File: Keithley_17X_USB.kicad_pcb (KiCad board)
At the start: 2 copper layers, 70.5 x 44 mm, 42 parts, among them J1 USB_B, J2 SIGNAL INPUT, J3 PROG, U1 TLP281-4, U2 TLP281-4, U3 MIC5504-3.3YM5, U4 MSP430FR2110, U5 FT230XS

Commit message: update silkscreen
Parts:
- added G***: LOGO, PL_logo:logo_height_10mm, F.Cu at (98.5, 82.0)
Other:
- board text added: "*"
- board text added: "5V"
- board text added: "Keithley 17X USB Adapter"
- board text added: "Keithley J1008 Connection"
- board text added: "March 2019"
- board text added: "RX"
- board text added: "TX"
- board text added: "github.com/sdp8483/Keithley_17X_USB"
- board text removed: "To Keithley J1008"

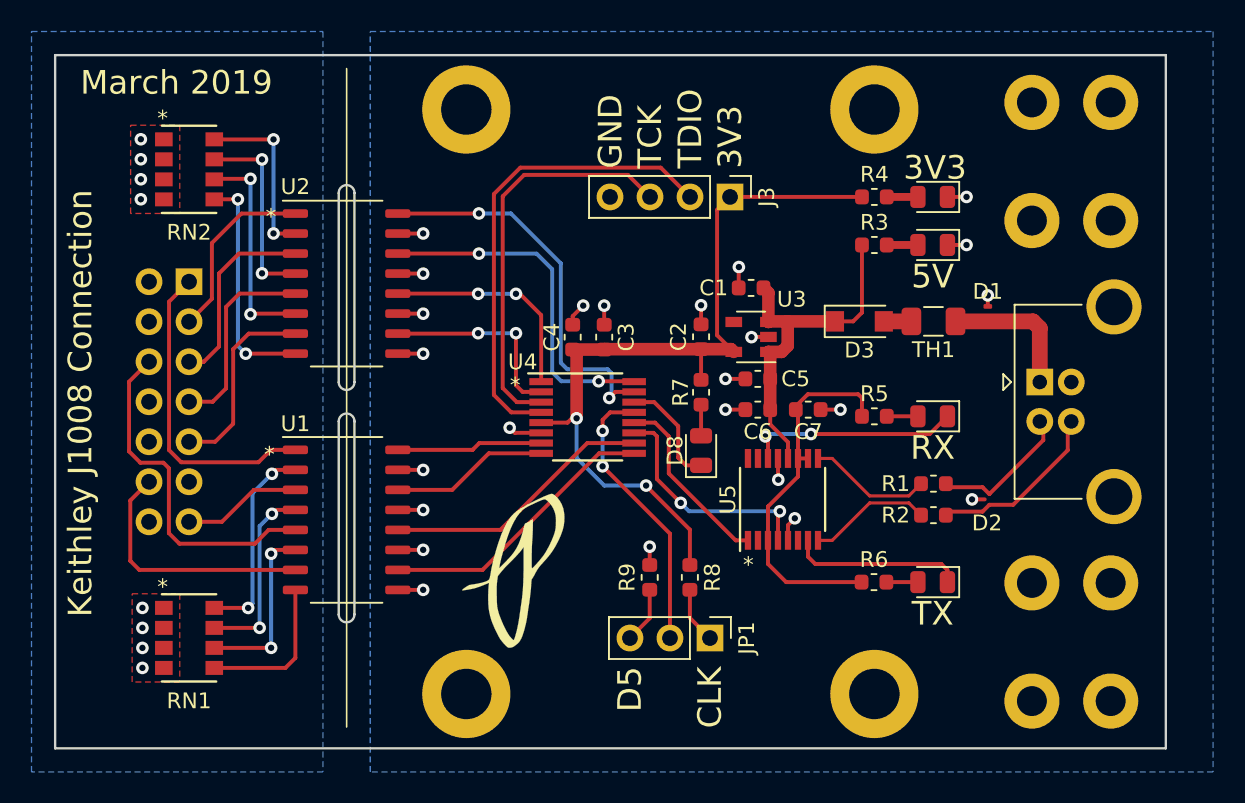
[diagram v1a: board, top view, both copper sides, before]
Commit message: minor silkscreen cleanup
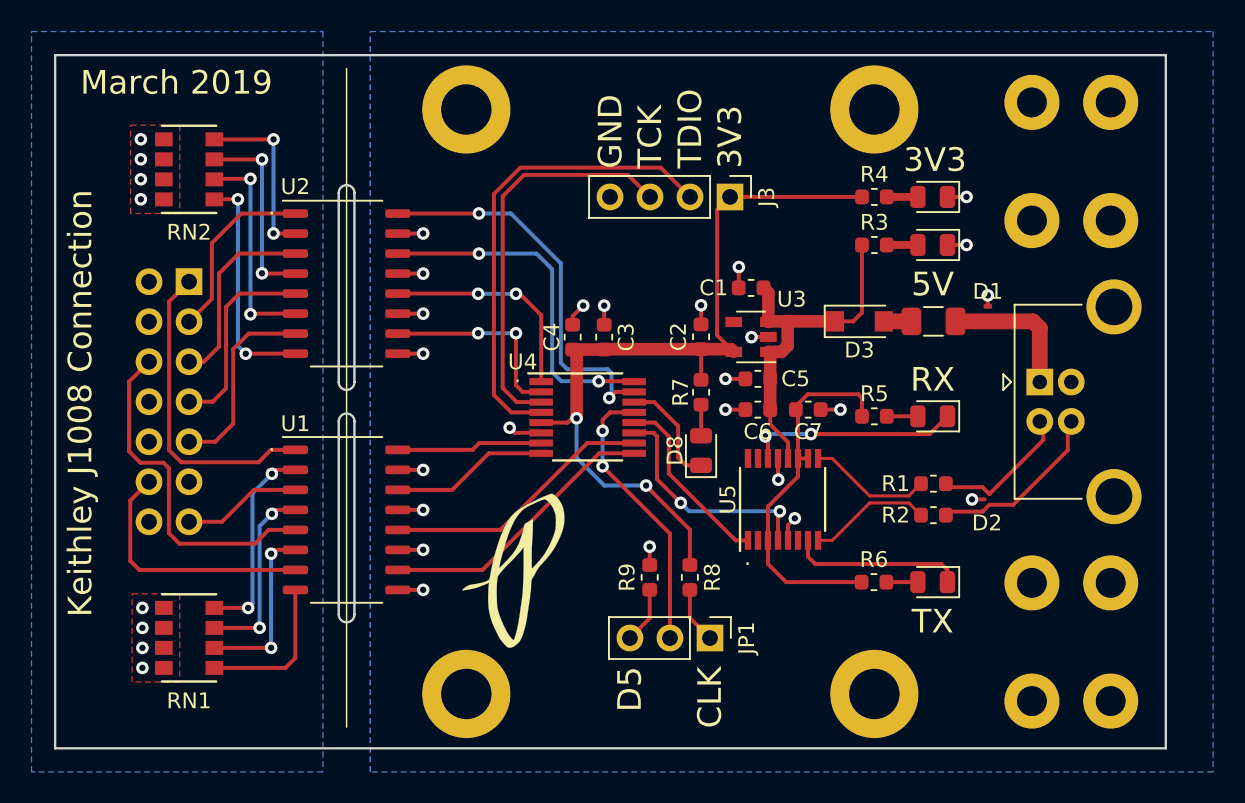
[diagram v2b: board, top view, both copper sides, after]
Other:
- board text added: "."
- board text added: "Sam Perry"
- board text removed: "*"
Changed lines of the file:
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@@
   (general
     (thickness 1.6)
-    (drawings 140)
+    (drawings 141)
     (tracks 375)
     (zones 0)
@@
   )
   (setup
-    (last_trace_width 0.5)
+    (last_trace_width 0.25)
     (user_trace_width 0.5)
     (user_trace_width 0.8)
@@
       (effects (font (size 0.127 0.127) (thickness 0.002)))
     )
-    (fp_text user * (at -1.6764 -3.2385) (layer F.SilkS)
+    (fp_text user * (at -1.6764 -3.2385) (layer F.SilkS) hide
       (effects (font (size 1 1) (thickness 0.15)))
     )
@@
       (effects (font (size 1 1) (thickness 0.15)))
     )
-    (fp_text user * (at -1.6764 -3.2385) (layer F.SilkS)
+    (fp_text user * (at -1.6764 -3.2385) (layer F.SilkS) hide
       (effects (font (size 1 1) (thickness 0.15)))
     )
@@
     (tags resistor)
     (attr smd)
-    (fp_text reference TH1 (at 0 1.8) (layer F.SilkS)
+    (fp_text reference TH1 (at 0 0) (layer F.SilkS) hide
       (effects (font (size 1 1) (thickness 0.15)))
     )
@@
       (xy 2.424964 -4.901719) (xy 2.473487 -4.908822) (xy 2.555224 -4.885326)) (layer F.SilkS) (width 0.01))
   )
-  (gr_text * (at 83.1 74.6) (layer F.SilkS)
+  (gr_text "Sam Perry" (at 76.3 91.1) (layer B.SilkS)
+    (effects (font (size 1.5 1.5) (thickness 0.3)) (justify mirror))
+  )
+  (gr_text . (at 83.25 73.9) (layer F.SilkS)
     (effects (font (size 1 1) (thickness 0.25)))
   )
-  (gr_text * (at 83.2 59.5) (layer F.SilkS)
+  (gr_text . (at 83.25 58.9) (layer F.SilkS)
     (effects (font (size 1 1) (thickness 0.25)))
   )
@@
     (effects (font (size 1.2 1.2) (thickness 0.17)) (justify mirror))
   )
-  (gr_text * (at 113.5 81.6) (layer F.SilkS)
+  (gr_text . (at 113.45 81.15) (layer F.SilkS)
     (effects (font (size 1 1) (thickness 0.25)))
   )
-  (gr_text * (at 98.7 70.2) (layer F.SilkS)
+  (gr_text . (at 98.85 69.55) (layer F.SilkS)
     (effects (font (size 1 1) (thickness 0.25)))
   )
@@
     (effects (font (size 1.5 1.5) (thickness 0.3)))
   )
-  (gr_text 3V3 (at 125.35 56.4) (layer F.SilkS)
+  (gr_text 3V3 (at 125.35 55.9) (layer F.SilkS)
     (effects (font (size 1.5 1.5) (thickness 0.3)))
   )
-  (gr_text 5V (at 125.2 63.3) (layer F.SilkS)
+  (gr_text 5V (at 125.2 63.8) (layer F.SilkS)
     (effects (font (size 1.5 1.5) (thickness 0.3)))
   )
-  (gr_text RX (at 125.2 74.175) (layer F.SilkS)
+  (gr_text RX (at 125.2 69.85) (layer F.SilkS)
     (effects (font (size 1.5 1.5) (thickness 0.3)))
   )
-  (gr_text TX (at 125.2 84.7) (layer F.SilkS)
+  (gr_text TX (at 125.2 85.2) (layer F.SilkS)
     (effects (font (size 1.5 1.5) (thickness 0.3)))
   )

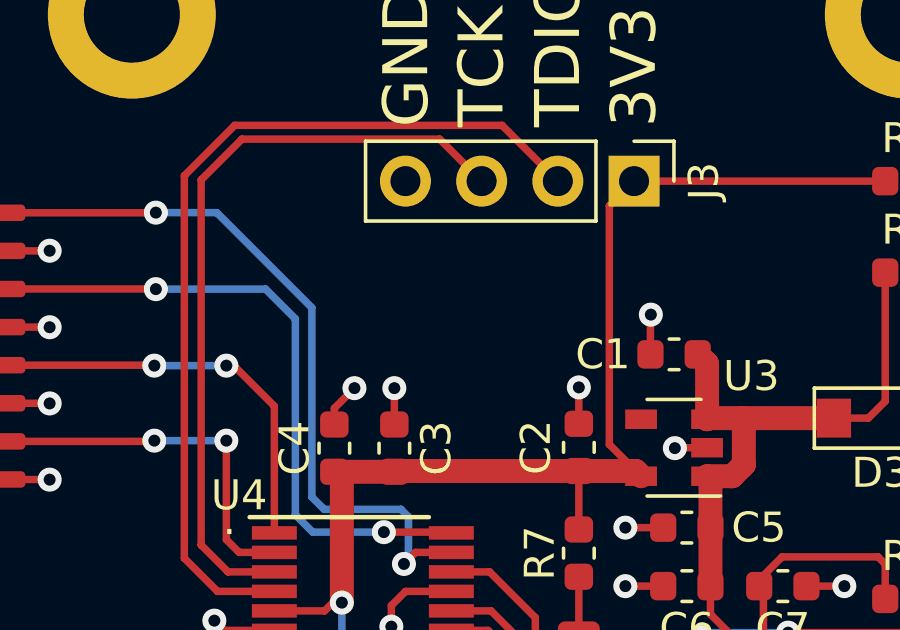
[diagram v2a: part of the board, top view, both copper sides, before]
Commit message: add bluebird logo
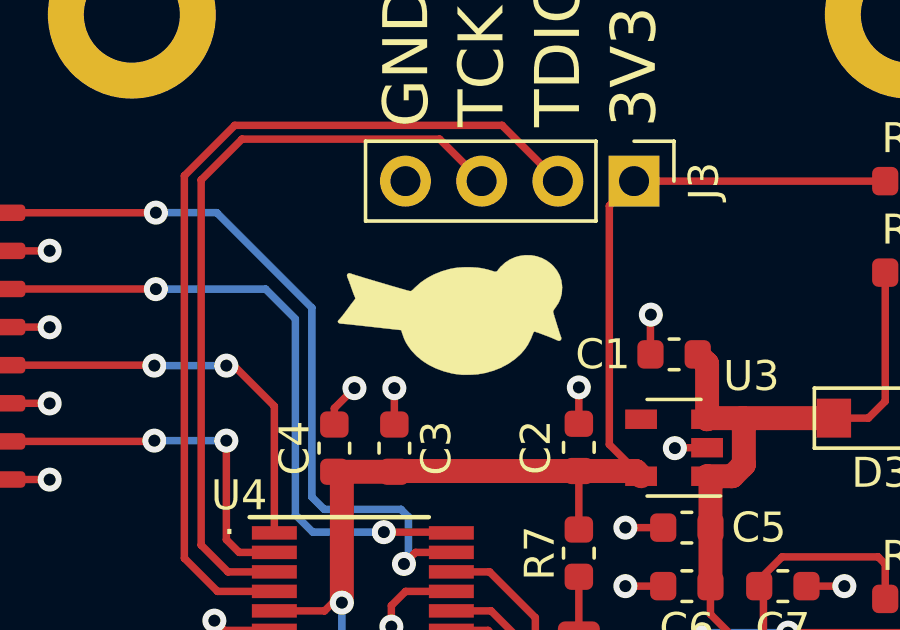
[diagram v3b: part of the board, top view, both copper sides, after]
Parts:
- added G***: LOGO, BB_logo:BB_logo_HxW_4x7.5mm, F.Cu at (106.2, 62.7)
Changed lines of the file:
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@@
     (tracks 375)
     (zones 0)
-    (modules 43)
+    (modules 44)
     (nets 51)
   )
@@
       (xy 2.424964 -4.901719) (xy 2.473487 -4.908822) (xy 2.555224 -4.885326)) (layer F.SilkS) (width 0.01))
   )
+  (module BB_logo:BB_logo_HxW_4x7.5mm (layer F.Cu)
+    (at 106.2 62.7)
+    (fp_text reference G*** (at 0 0) (layer F.SilkS) hide
+      (effects (font (size 1.524 1.524) (thickness 0.3)))
+    )
+    (fp_text value LOGO (at 0.75 0) (layer F.SilkS) hide
+      (effects (font (size 1.524 1.524) (thickness 0.3)))
+    )
+    (fp_poly (pts (xy 2.713927 -1.978373) (xy 2.895506 -1.945528) (xy 3.070555 -1.885268) (xy 3.235321 -1.797572)
+      (xy 3.38605 -1.682422) (xy 3.459178 -1.610019) (xy 3.577218 -1.461306) (xy 3.662911 -1.304796)
+      (xy 3.717434 -1.137514) (xy 3.741962 -0.956484) (xy 3.743678 -0.889961) (xy 3.73089 -0.709742)
+      (xy 3.691076 -0.545202) (xy 3.622063 -0.390068) (xy 3.521675 -0.23807) (xy 3.514363 -0.2286)
+      (xy 3.465913 -0.159606) (xy 3.443954 -0.111185) (xy 3.443268 -0.093134) (xy 3.45579 -0.045345)
+      (xy 3.475787 0.024796) (xy 3.501503 0.111666) (xy 3.531183 0.209644) (xy 3.56307 0.313107)
+      (xy 3.595407 0.416431) (xy 3.626438 0.513995) (xy 3.654407 0.600176) (xy 3.677557 0.669352)
+      (xy 3.694133 0.715899) (xy 3.701189 0.732569) (xy 3.718155 0.788501) (xy 3.704623 0.836223)
+      (xy 3.671061 0.865458) (xy 3.640667 0.874227) (xy 3.603186 0.866306) (xy 3.566375 0.849917)
+      (xy 3.511462 0.824622) (xy 3.437823 0.793194) (xy 3.350839 0.757671) (xy 3.255891 0.720093)
+      (xy 3.158361 0.682501) (xy 3.063629 0.646933) (xy 2.977078 0.615428) (xy 2.904088 0.590028)
+      (xy 2.850041 0.572771) (xy 2.820318 0.565696) (xy 2.816927 0.565872) (xy 2.791362 0.588472)
+      (xy 2.78272 0.604982) (xy 2.699594 0.814185) (xy 2.604955 0.996877) (xy 2.494918 1.159546)
+      (xy 2.365602 1.308678) (xy 2.35488 1.319637) (xy 2.162621 1.49097) (xy 1.946322 1.640562)
+      (xy 1.70905 1.766977) (xy 1.453869 1.86878) (xy 1.183844 1.944537) (xy 0.922867 1.990257)
+      (xy 0.881116 1.993977) (xy 0.818728 1.997654) (xy 0.742836 2.001076) (xy 0.660579 2.004033)
+      (xy 0.579091 2.006315) (xy 0.505508 2.007712) (xy 0.446966 2.008013) (xy 0.410602 2.007008)
+      (xy 0.402284 2.005602) (xy 0.384538 2.002058) (xy 0.342368 1.99674) (xy 0.287867 1.991091)
+      (xy 0.209951 1.982986) (xy 0.148141 1.974394) (xy 0.084743 1.962714) (xy 0.059267 1.957492)
+      (xy -0.212679 1.886623) (xy -0.468415 1.791356) (xy -0.70548 1.673184) (xy -0.921417 1.533601)
+      (xy -1.113767 1.374101) (xy -1.28007 1.196178) (xy -1.353962 1.098968) (xy -1.425221 0.992841)
+      (xy -1.480046 0.897149) (xy -1.525512 0.797946) (xy -1.568693 0.68129) (xy -1.574311 0.6647)
+      (xy -1.62412 0.516467) (xy -2.560426 0.411862) (xy -2.737333 0.392194) (xy -2.906057 0.37362)
+      (xy -3.063241 0.356499) (xy -3.20553 0.341185) (xy -3.329567 0.328038) (xy -3.431995 0.317413)
+      (xy -3.509459 0.309667) (xy -3.558603 0.305158) (xy -3.572933 0.304161) (xy -3.642429 0.299177)
+      (xy -3.686346 0.289305) (xy -3.712906 0.271806) (xy -3.725739 0.253241) (xy -3.733294 0.237121)
+      (xy -3.73358 0.222119) (xy -3.722985 0.202303) (xy -3.697897 0.171739) (xy -3.654703 0.124496)
+      (xy -3.633408 0.1016) (xy -3.610839 0.074621) (xy -3.572247 0.025572) (xy -3.521651 -0.040315)
+      (xy -3.46307 -0.11781) (xy -3.405674 -0.194734) (xy -3.343714 -0.277973) (xy -3.286539 -0.354184)
+      (xy -3.238048 -0.418216) (xy -3.202139 -0.464921) (xy -3.183469 -0.488272) (xy -3.157571 -0.523296)
+      (xy -3.152092 -0.552961) (xy -3.166033 -0.591778) (xy -3.175108 -0.609809) (xy -3.189214 -0.642247)
+      (xy -3.211763 -0.700115) (xy -3.240274 -0.776785) (xy -3.272267 -0.865629) (xy -3.29365 -0.926468)
+      (xy -3.32674 -1.019935) (xy -3.358165 -1.105764) (xy -3.38539 -1.177244) (xy -3.405879 -1.227668)
+      (xy -3.414294 -1.245802) (xy -3.429565 -1.301025) (xy -3.417527 -1.345885) (xy -3.384447 -1.374427)
+      (xy -3.336595 -1.380696) (xy -3.289502 -1.364355) (xy -3.266789 -1.355857) (xy -3.21509 -1.338991)
+      (xy -3.137954 -1.314805) (xy -3.038924 -1.28435) (xy -2.921549 -1.248675) (xy -2.789372 -1.208829)
+      (xy -2.645941 -1.165862) (xy -2.494802 -1.120825) (xy -2.339501 -1.074766) (xy -2.183582 -1.028734)
+      (xy -2.030594 -0.983781) (xy -1.884081 -0.940954) (xy -1.747591 -0.901305) (xy -1.624667 -0.865882)
+      (xy -1.518858 -0.835735) (xy -1.433708 -0.811914) (xy -1.372765 -0.795468) (xy -1.342385 -0.788017)
+      (xy -1.315443 -0.784384) (xy -1.291387 -0.789168) (xy -1.263677 -0.806436) (xy -1.225776 -0.840252)
+      (xy -1.171602 -0.89422) (xy -0.981618 -1.063615) (xy -0.767066 -1.212752) (xy -0.531952 -1.339549)
+      (xy -0.280286 -1.441922) (xy -0.016073 -1.517789) (xy 0.059267 -1.53393) (xy 0.103674 -1.542766)
+      (xy 0.134866 -1.548987) (xy 0.239919 -1.564385) (xy 0.36908 -1.57468) (xy 0.51298 -1.579868)
+      (xy 0.662246 -1.579949) (xy 0.807508 -1.574917) (xy 0.939395 -1.564772) (xy 1.048534 -1.549509)
+      (xy 1.049867 -1.549257) (xy 1.25383 -1.504386) (xy 1.426064 -1.45359) (xy 1.487974 -1.435227)
+      (xy 1.528947 -1.430915) (xy 1.557297 -1.439029) (xy 1.584321 -1.458797) (xy 1.591734 -1.471347)
+      (xy 1.60248 -1.489162) (xy 1.631289 -1.52535) (xy 1.673017 -1.573619) (xy 1.697567 -1.600808)
+      (xy 1.839487 -1.732046) (xy 1.997401 -1.835986) (xy 2.167557 -1.912608) (xy 2.346199 -1.961893)
+      (xy 2.529574 -1.983821) (xy 2.713927 -1.978373)) (layer F.SilkS) (width 0.01))
+  )
   (gr_text "Sam Perry" (at 76.3 91.1) (layer B.SilkS)
